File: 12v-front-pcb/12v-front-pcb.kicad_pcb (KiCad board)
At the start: 2 copper layers, 94.7 x 98.8 mm, 24 parts, among them J1 76825-0002, J2 76825-0004, J3 76825-0004, J4 76825-0004, J5 76825-0002, J6 76825-0004, J7 76825-0002

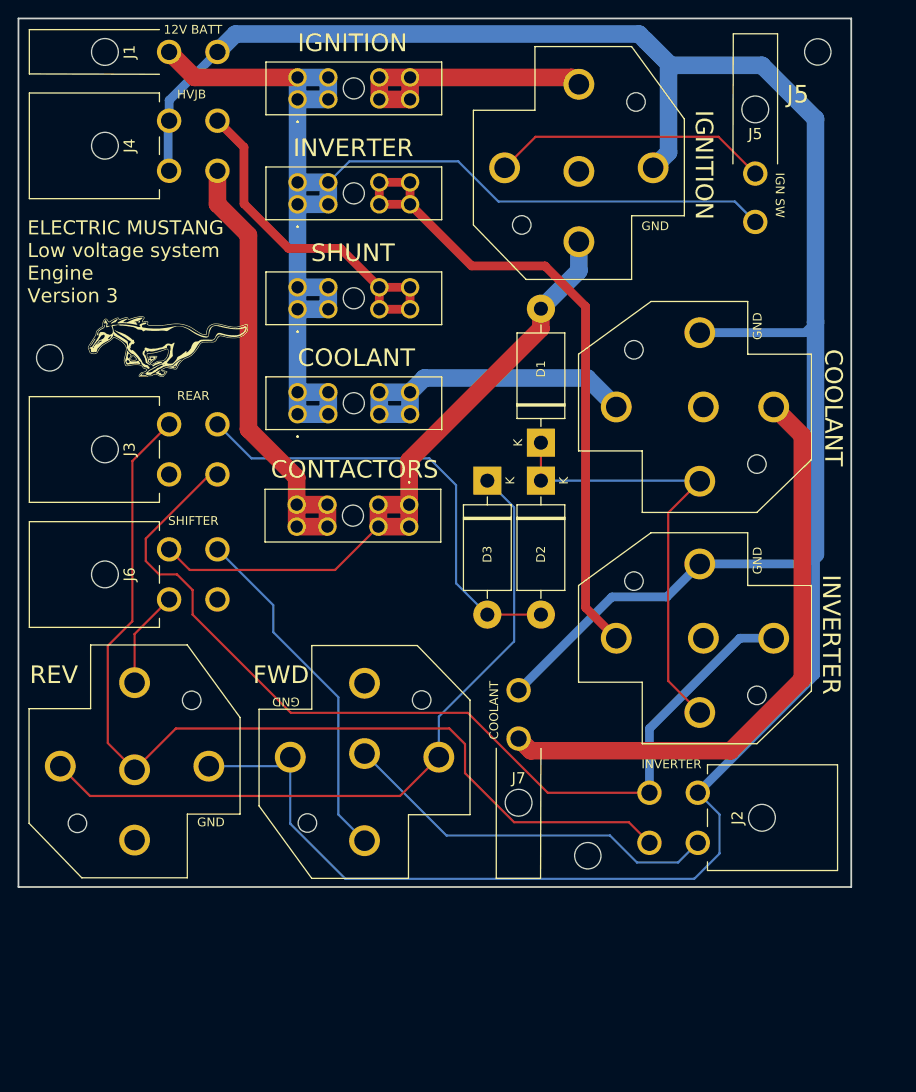
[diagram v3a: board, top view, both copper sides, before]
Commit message: Rework front PCB to make more room for relays
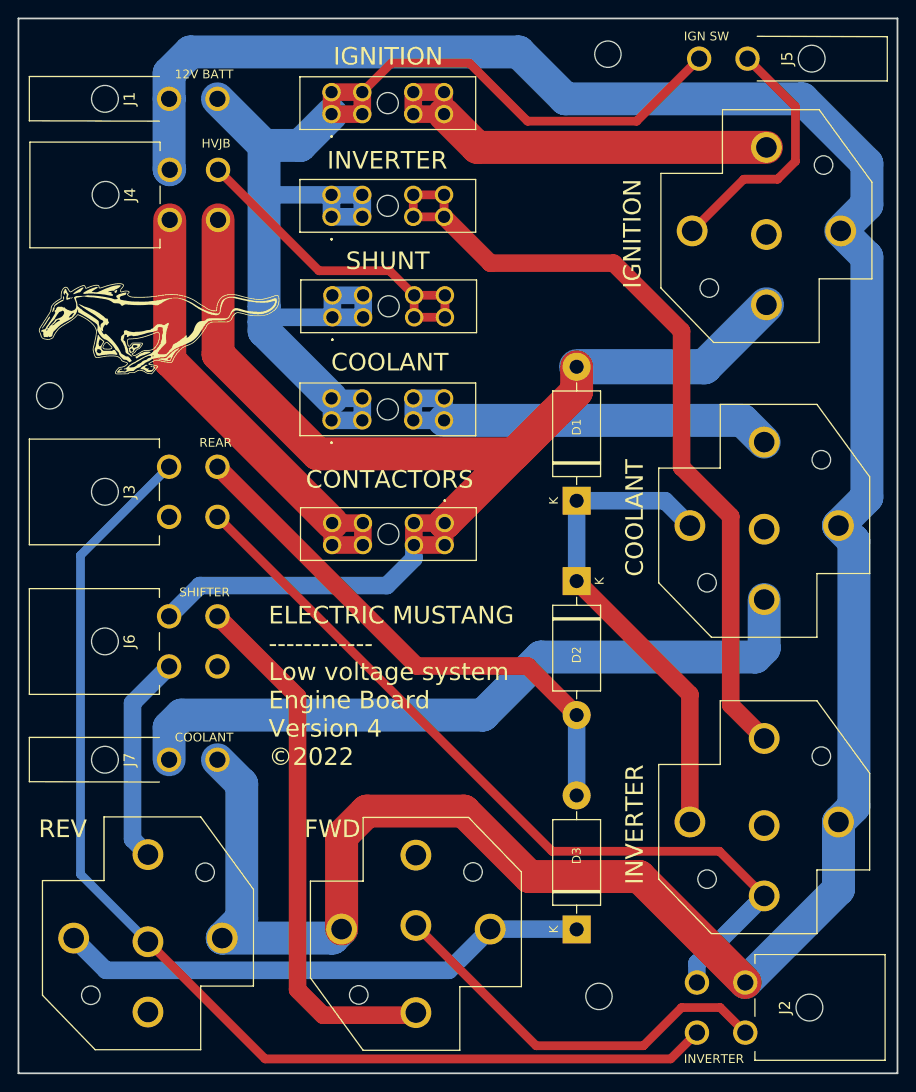
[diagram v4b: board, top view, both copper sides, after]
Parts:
- moved D3 52.1 mm to (214.1, 195.8), turned to 90 degrees
- moved J7 45.0 mm to (162.6, 176.5), turned to -90 degrees
- moved INVERTER_RELAY1 29.3 mm to (235.5, 192.0), turned to 90 degrees
- moved H2 23.9 mm to (217.7, 96.3)
- moved IGNITION_RELAY1 22.5 mm to (235.7, 124.8)
- moved J2 22.3 mm to (238.5, 204.7)
- moved COOLANT_PUMP_RELAY1 21.9 mm to (235.5, 158.3), turned to 90 degrees
- moved FWD_DRIVE_INHIBIT_RELAY1 20.4 mm to (195.8, 187.4)
- moved REV_DRIVE_INHIBIT_RELAY1 19.6 mm to (165.4, 205.2)
- moved H4 16.1 mm to (216.7, 203.5)
- moved D2 12.1 mm to (214.1, 156.2)
- moved J5 8.98 mm to (238.8, 96.8), turned to 90 degrees
- moved D1 7.75 mm to (214.1, 147.1)
- moved J6 7.62 mm to (162.6, 163.1)
- moved J4 5.59 mm to (162.6, 112.3)
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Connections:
- net INVERTER_12V renamed IGNITION_ENABLE_OUT
- J1 pad 1: CONTACTORS_GND -> 12V_BATT_IN
- J1 pad 2: 12V_BATT_IN -> CONTACTORS_GND
- J4 pad 2: CONTACTORS_12V -> IGNITION_12V
- J4 pad 4: CONTACTORS_GND -> CONTACTORS_12V
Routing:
- net IGNITION_12V: track 76.7 -> 152.6 mm
- net Net-(D3-Pad1): track 82.6 -> 60.7 mm
- net SHIFTER_FWD: track 40.1 -> 61.0 mm
- net INVERTER_REV: track 111.3 -> 130.6 mm
- net Net-(IGNITION_FUSE1-Pad3): track 31.5 -> 50.2 mm
- net Net-(INVERTER_FUSE1-Pad3): track 76.0 -> 94.6 mm
- net CONTACTORS_GND: track 318.8 -> 301.6 mm
- net IGNITION_ENABLE_OUT: track 109.3 -> 93.1 mm
- net 12V_BATT_IN: track 144.2 -> 158.5 mm
- net SHIFTER_REV: track 11.1 -> 23.9 mm
- net COOLANT_12V: track 68.5 -> 80.6 mm
- net Net-(COOLANT_PUMP_FUSE1-Pad3): track 37.5 -> 49.4 mm
- net CHARGER_ENABLE_IN: track 52.3 -> 61.7 mm
- net Net-(COOLANT_PUMP_RELAY1-Pad4): track 51.7 -> 55.9 mm
- net IGNITION_SWITCH_B: track 31.7 -> 29.0 mm
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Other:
- board size 94.7 x 98.8 mm -> 100 x 120 mm
- board text added: "ELECTRIC MUSTANG ------------ Low voltage system Engine Board Version 4 ©2022"
- board text removed: "ELECTRIC MUSTANG Low voltage system Engine Version 3"
- board text removed: "GND"
- board text removed: "J5"

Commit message: Updates to the 12v front pcb
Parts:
- added BRAKE_FUSE1: 178.6165.0001, Socket:17861650001, F.Cu at (305.0, 187.3)
- added CHARGING_CONTACTORS1: DZ85AB-5-PCB, Connector:DZ85AB5PCB, F.Cu at (275.0, 165.0)
- added CHARGING_CONTACTORS_FUSE1: 178.6165.0001, Socket:17861650001, F.Cu at (250.7, 127.0)
- added FRONT_BATTERY_INHIBIT1: DZ85AB-5-PCB, Connector:DZ85AB5PCB, F.Cu at (310.0, 165.0)
- added J10: 76825-0002, Connector:768250002, F.Cu at (325.1, 134.1)
- added J8: 76825-0004, Connector:768250004, F.Cu at (342.6, 134.0)
- added J9: 76825-0004, Connector:768250004, F.Cu at (308.4, 134.0)
- added REAR_BATTERY_INHIBIT1: DZ85AB-5-PCB, Connector:DZ85AB5PCB, F.Cu at (345.0, 165.0)
- moved G*** 211.5 mm to (362.5, 47.8)
- moved H3 202.3 mm to (336.3, 47.0)
- moved H4 183.7 mm to (336.3, 64.0)
- moved J2 140.5 mm to (117.6, 133.1), turned to 180 degrees
- moved H2 125.6 mm to (336.3, 55.1)
- moved J4 120.8 mm to (281.4, 134.0), turned to 180 degrees
- moved CONTACTORS_FUSE1 89.1 mm to (279.9, 187.3), turned to 0 degrees
- moved J6 83.4 mm to (85.6, 131.1), turned to 180 degrees
- moved J1 80.5 mm to (236.0, 134.4), turned to 180 degrees
- moved ISA_SHUNT_FUSE1 77.3 mm to (263.7, 127.0), turned to -90 degrees
- moved REV_DRIVE_INHIBIT_RELAY1 76.7 mm to (100.0, 165.0), turned to 180 degrees
- moved INVERTER_RELAY1 70.8 mm to (170.0, 165.0), turned to 180 degrees
- moved FWD_DRIVE_INHIBIT_RELAY1 64.8 mm to (135.0, 165.0), turned to 180 degrees
- moved J7 52.5 mm to (193.3, 134.0), turned to 180 degrees
- moved J5 49.6 mm to (206.0, 134.0), turned to 180 degrees
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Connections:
- J1 pad 1: 12V_BATT_IN -> CONTACTORS_GND
- J1 pad 2: CONTACTORS_GND -> 12V_BATT_IN
- J4 pad 3: CONTACTORS_GND -> HVJB_GND
- J5 pad 1: 12V_BATT_IN -> IGNITION_SWITCH_B
- J5 pad 2: IGNITION_SWITCH_B -> 12V_BATT_IN
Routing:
- net FRONT_BATTERY_12V: track 0.00 -> 139.1 mm
- net INVERTER_REV: track 130.6 -> 0.00 mm
- net IGNITION_12V: track 152.6 -> 29.5 mm
- net Net-(COOLANT_PUMP_RELAY1-Pad4): track 55.9 -> 173.4 mm
- net Net-(CHARGING_CONTACTORS1-Pad4): track 60.7 -> 156.8 mm
- net IGNITION_ENABLE_OUT: track 93.1 -> 0.00 mm
- net SHIFTER_FWD: track 61.0 -> 0.00 mm
- net Net-(INVERTER_FUSE1-Pad3): track 94.6 -> 38.0 mm
- net CONTACTORS_12V: track 54.2 -> 0.00 mm
- net COOLANT_12V: track 80.6 -> 32.9 mm
- net INVERTER_FWD: track 46.1 -> 0.00 mm
- net ISA_SHUNT_12V: track 40.2 -> 0.00 mm
- net Net-(CHARGING_CONTACTORS1-Pad3): track 0.00 -> 29.3 mm
- net CONTACTORS_GND: track 301.6 -> 325.9 mm
- net SHIFTER_REV: track 23.9 -> 0.00 mm
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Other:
- board size 100 x 120 mm -> 128 x 121.7 mm
- board text added: "12V"
- board text added: "BRAKE"
- board text added: "CHARGE CONT"
- board text added: "COOLANT PUMP"
- board text added: "FRONT BATT"
- board text added: "ISA"
- board text added: "REAR BATT"

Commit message: Errors in charge/drive mode
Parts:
- removed J8, J9: 76825-0004, Connector:768250004
- added CRUISE_FUSE1: 178.6165.0001, Library:17861650001, F.Cu at (139.7, 171.1)
- added D4: 1N5406, Diode_THT:D_DO-201AD_P15.24mm_Horizontal, F.Cu at (211.8, 183.1)
- added J11: 76825-0002, Library:768250002, F.Cu at (212.6, 225.5)
- added J12: 76825-0002, Library:768250002, F.Cu at (371.1, 162.7)
- added J14: 76825-0002, Library:768250002, F.Cu at (259.6, 225.7)
- added J15: 76825-0002, Library:768250002, F.Cu at (271.2, 225.7)
- BRAKE_FUSE1, CHARGING_CONTACTORS_FUSE1, CONTACTORS_FUSE1, COOLANT_PUMP_FUSE1, IGNITION_FUSE1, INVERTER_FUSE1, ISA_SHUNT_FUSE1: footprint Socket:17861650001 -> Library:17861650001
- CHARGING_CONTACTORS1, COOLANT_PUMP_RELAY1, FRONT_BATTERY_INHIBIT1, FWD_DRIVE_INHIBIT_RELAY1, IGNITION_RELAY1, INVERTER_RELAY1, REAR_BATTERY_INHIBIT1, REV_DRIVE_INHIBIT_RELAY1: footprint Connector:DZ85AB5PCB -> Library:DZ85AB5PCB
- J1, J10, J7: footprint Connector:768250002 -> Library:768250002
- J2, J3, J4, J6: footprint Connector:768250004 -> Library:768250004
- J5: value 76825-0002 -> 76825-0004; footprint Connector:768250002 -> Library:768250004
- moved J10 138.1 mm to (221.7, 225.7), turned to 0 degrees
- moved J6 120.3 mm to (162.3, 223.7), turned to 0 degrees
- moved REAR_BATTERY_INHIBIT1 113.5 mm to (235.4, 194.4), turned to 0 degrees
- moved J3 90.8 mm to (144.0, 224.0), turned to 0 degrees
- moved BRAKE_FUSE1 83.2 mm to (221.8, 185.7), turned to -90 degrees
- moved REV_DRIVE_INHIBIT_RELAY1 82.4 mm to (176.9, 194.6), turned to 0 degrees
- moved FRONT_BATTERY_INHIBIT1 49.4 mm to (270.4, 194.4), turned to 0 degrees
- moved FWD_DRIVE_INHIBIT_RELAY1 30.4 mm to (141.9, 194.6), turned to 0 degrees
- moved D2 26.6 mm to (178.6, 158.0), turned to -90 degrees
- moved D1 26.4 mm to (213.6, 157.5), turned to -90 degrees
- moved J2 20.1 mm to (137.7, 134.4)
- moved D3 19.8 mm to (205.2, 198.4), turned to 90 degrees
- moved CONTACTORS_FUSE1 19.0 mm to (289.8, 171.1), turned to 90 degrees
- moved IGNITION_FUSE1 7.92 mm to (226.9, 126.8)
- moved J5 5.85 mm to (211.8, 133.7)
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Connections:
- CHARGING_CONTACTORS1 pad 1: FRONT_BATTERY_12V -> CHG_CONTACTOR_POS_12V
- COOLANT_PUMP_RELAY1 pad 4: Net-(COOLANT_PUMP_RELAY1-Pad4) -> Net-(D1-Pad1)
- D1 pad 1: Net-(COOLANT_PUMP_RELAY1-Pad4) -> Net-(D1-K)
- D2 pad 1: Net-(COOLANT_PUMP_RELAY1-Pad4) -> Net-(D1-K)
- D3 pad 1: Net-(CHARGING_CONTACTORS1-Pad4) -> Net-(D3-K)
- FRONT_BATTERY_INHIBIT1 pad 3: Net-(COOLANT_PUMP_RELAY1-Pad4) -> Net-(D1-Pad1)
- FRONT_BATTERY_INHIBIT1 pad 4: Net-(CHARGING_CONTACTORS1-Pad4) -> unconnected-(FRONT_BATTERY_INHIBIT1-Pad4)
- FWD_DRIVE_INHIBIT_RELAY1 pad 4: Net-(CHARGING_CONTACTORS1-Pad4) -> DRIVE_INHIBIT
- INVERTER_RELAY1 pad 4: Net-(COOLANT_PUMP_RELAY1-Pad4) -> Net-(D1-Pad1)
- J2 pad 1: INVERTER_REV -> BRAKE_SWITCH_RETURN
- J3 pad 3: INVERTER_REV -> BRAKE_SWITCH_RETURN
- J4 pad 1: ISA_SHUNT_12V -> IGNITION_12V
- J4 pad 2: IGNITION_12V -> ISA_SHUNT_12V
- REAR_BATTERY_INHIBIT1 pad 2: FRONT_BATTERY_12V -> REAR_BATTERY_12V
- REAR_BATTERY_INHIBIT1 pad 3: Net-(COOLANT_PUMP_RELAY1-Pad4) -> Net-(D1-Pad1)
- REAR_BATTERY_INHIBIT1 pad 4: Net-(CHARGING_CONTACTORS1-Pad4) -> unconnected-(REAR_BATTERY_INHIBIT1-Pad4)
- REV_DRIVE_INHIBIT_RELAY1 pad 2: INVERTER_REV -> BRAKE_SWITCH_RETURN
- REV_DRIVE_INHIBIT_RELAY1 pad 4: Net-(CHARGING_CONTACTORS1-Pad4) -> DRIVE_INHIBIT
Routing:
- net CONTACTORS_GND: track 325.9 -> 133.1 mm
- net Net-(COOLANT_PUMP_RELAY1-Pad4): track 173.4 -> 0.00 mm
- net Net-(CHARGING_CONTACTORS1-Pad4): track 156.8 -> 0.00 mm
- net FRONT_BATTERY_12V: track 139.1 -> 23.6 mm
- net Net-(D1-Pad1): track 0.00 -> 98.1 mm
- net IGNITION_12V: track 29.5 -> 85.2 mm
- net CHARGER_ENABLE_IN: track 39.7 -> 0.00 mm
- net IGNITION_SWITCH_B: track 46.6 -> 8.61 mm
- net Net-(D1-K): track 0.00 -> 37.4 mm
- net REAR_BATTERY_12V: track 0.00 -> 29.9 mm
- net 12V_BATT_IN: track 137.5 -> 113.1 mm
- net ISA_SHUNT_12V: track 0.00 -> 12.9 mm
- net REAR_BATTERY_INHIBIT: track 15.5 -> 28.0 mm
- net FRONT_BATTERY_INHIBIT: track 15.8 -> 20.8 mm
- net Net-(IGNITION_FUSE1-Pad3): track 29.0 -> 27.4 mm
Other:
- board size 128 x 121.7 mm -> 338.8 x 160.1 mm

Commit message: rework on 12v front pcb
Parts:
- removed H2, H3, H4: MountingHole, MountingHole:MountingHole_3mm
- added D5: LED, LED_THT:LED_D3.0mm_Clear, F.Cu at (188.5, 186.7)
- added D6: LED, LED_THT:LED_D3.0mm_Clear, F.Cu at (188.5, 191.5)
- added DASH_FUSE1: 178.6165.0001, Library:17861650001, F.Cu at (80.0, 178.6)
- added J8: 76825-0004, Library:768250004, F.Cu at (92.8, 210.1)
- added J9: 76825-0004, Library:768250004, F.Cu at (165.0, 210.0)
- added R1: R_US, Diode_THT:D_T-1_P2.54mm_Vertical_AnodeUp, F.Cu at (196.5, 186.6)
- added R2: R_US, Diode_THT:D_T-1_P2.54mm_Vertical_AnodeUp, F.Cu at (196.6, 191.4)
- added WIPER_FUSE1: 178.6165.0001, Library:17861650001, F.Cu at (120.0, 187.0)
- moved G*** 200.4 mm to (219.2, 188.0)
- moved ISA_SHUNT_FUSE1 184.1 mm to (80.0, 139.1), turned to 0 degrees
- moved J1 177.8 mm to (79.0, 210.0), turned to 0 degrees
- moved CHARGING_CONTACTORS_FUSE1 174.9 mm to (80.0, 165.3), turned to 0 degrees
- moved CONTACTORS_FUSE1 148.0 mm to (142.7, 154.3), turned to 0 degrees
- moved IGNITION_FUSE1 146.9 mm to (80.0, 126.0), turned to 0 degrees
- moved J12 137.5 mm to (242.0, 210.0)
- moved J5 119.0 mm to (120.6, 210.0), turned to 0 degrees
- moved IGNITION_RELAY1 117.2 mm to (127.0, 134.0)
- moved J7 115.4 mm to (106.5, 210.0), turned to 0 degrees
- moved J4 110.3 mm to (200.0, 210.0), turned to 0 degrees
- moved COOLANT_PUMP_FUSE1 102.7 mm to (80.0, 152.2), turned to 0 degrees
- moved INVERTER_FUSE1 98.8 mm to (79.5, 191.9), turned to 0 degrees
- moved BRAKE_FUSE1 98.6 mm to (142.7, 126.9), turned to 0 degrees
- moved FWD_DRIVE_INHIBIT_RELAY1 91.8 mm to (210.5, 133.5)
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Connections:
- net FRONT_BATTERY_12V renamed FRONT_BATTERY_ENABLE
- net REAR_BATTERY_12V renamed REAR_BATTERY_ENABLE
- CHARGING_CONTACTORS1 pad 1: CHG_CONTACTOR_POS_12V -> CHG_CONTACTORS_12V
- CHARGING_CONTACTORS1 pad 4: Net-(CHARGING_CONTACTORS1-Pad4) -> Net-(D3-K)
- COOLANT_PUMP_RELAY1 pad 4: Net-(D1-Pad1) -> Net-(D1-K)
- FRONT_BATTERY_INHIBIT1 pad 3: Net-(D1-Pad1) -> Net-(D1-K)
- FRONT_BATTERY_INHIBIT1 pad 4: unconnected-(FRONT_BATTERY_INHIBIT1-Pad4) -> 12V_BATT_IN
- INVERTER_RELAY1 pad 4: Net-(D1-Pad1) -> Net-(D1-K)
- J10 pad 2: BRAKE_SWITCH_RETURN -> BRAKE_SIGNAL
- J11 pad 1: BRAKE_SWITCH_RETURN -> BRAKE_SIGNAL
- J2 pad 1: BRAKE_SWITCH_RETURN -> INVERTER_REV
- J3 pad 3: BRAKE_SWITCH_RETURN -> INVERTER_REV
- J3 pad 4: unconnected-(J3-Pad4) -> DRIVE_INHIBIT
- J4 pad 3: HVJB_GND -> CONTACTORS_12V
- J4 pad 4: CONTACTORS_12V -> HVJB_GND
- J7 pad 1: CONTACTORS_GND -> COOLANT_12V
- J7 pad 2: COOLANT_12V -> CONTACTORS_GND
- REAR_BATTERY_INHIBIT1 pad 3: Net-(D1-Pad1) -> Net-(D1-K)
- REAR_BATTERY_INHIBIT1 pad 4: unconnected-(REAR_BATTERY_INHIBIT1-Pad4) -> 12V_BATT_IN
- REV_DRIVE_INHIBIT_RELAY1 pad 2: BRAKE_SWITCH_RETURN -> INVERTER_REV
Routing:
- net 12V_BATT_IN: track 113.1 -> 544.3 mm
- net DRIVE_INHIBIT: track 0.00 -> 237.4 mm
- net IGNITION_12V: track 85.2 -> 321.1 mm, vias 0 -> 1
- net ISA_SHUNT_12V: track 12.9 -> 190.5 mm
- net Net-(D1-K): track 37.4 -> 206.7 mm
- net SHIFTER_FWD: track 0.00 -> 162.6 mm
- net SHIFTER_REV: track 0.00 -> 154.1 mm
- net CRUISE_BUTTON_RETURN: track 0.00 -> 149.5 mm
- net CONTACTORS_GND: track 133.1 -> 0.00 mm
- net INVERTER_FWD: track 0.00 -> 125.8 mm
- net CRUISE_BUTTON_SEND: track 0.00 -> 113.6 mm
- net INVERTER_REV: track 0.00 -> 110.9 mm
- net Net-(D3-K): track 0.00 -> 108.1 mm
- net Net-(D1-Pad1): track 98.1 -> 0.00 mm
- net BRAKE_SWITCH_SEND: track 0.00 -> 95.2 mm
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- added copper zone on F.Cu, net CONTACTORS_GND
- added copper zone on B.Cu, net HVJB_GND
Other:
- board size 338.8 x 160.1 mm -> 220 x 110 mm
- copper layers 2 -> 4
- board text added: "CHARGE ON"
- board text added: "CHRG CONT"
- board text added: "CRUISE"
- board text added: "DASH"
- board text added: "ELECTRIC MUSTANG Low voltage system Front Board Version 5 ©2023"
- board text added: "FORWARD"
- board text added: "IGN"
- board text added: "IGNITION ON"
- board text added: "J1 : 12V BATT"
- board text added: "J10 : BRAKE SW"
- board text added: "J11 : DASH3"
- board text added: "J12 : CHG CONT"
- board text added: "J14 : REAR BATT"
- board text added: "J15 : FRONT BATT"
- board text added: "J2 : INVERTER"
- board text added: "J3 : REAR"
- board text added: "J4 : HVJB"
- board text added: "J5 : DASH1"
- board text added: "J6 : SHIFTER"
- board text added: "J7 : COOLANT"
- board text added: "J8 : DASH2"
- board text added: "J9 : AUX IGN"
- board text added: "REVERSE"
- board text added: "WIPERS"
- board text removed: "12V"
- board text removed: "12V BATT"
- board text removed: "COOLANT PUMP"
- board text removed: "ELECTRIC MUSTANG ------------ Low voltage system Engine Board Version 4 ©2022"
- board text removed: "FWD"
- board text removed: "HVJB"
- board text removed: "IGN SW"
- board text removed: "ISA"
- board text removed: "REAR"
- board text removed: "REV"
- board text removed: "SHIFTER"
